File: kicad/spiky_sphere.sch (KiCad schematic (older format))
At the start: 0 parts

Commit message: filled in fixation target schematic
looks done... will review tomorrow
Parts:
- added JP? (x5): JUMPER, ~, symbol JUMPER
- added P?: CONN_8, ~, symbol CONN_8
- added U?: LED_MTX_5X7, symbol LED_MTX_5X7
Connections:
- new net: JP?.2, U?.2 (COL_1)
- new net: JP?.2, U?.1 (COL_2)
- new net: JP?.2, U?.4 (COL_3)
- new net: JP?.2, U?.9 (COL_4)
- new net: JP?.2, U?.7 (COL_5)
- new net fixation_target_module_1/GND: JP?.1, JP?.1, JP?.1, JP?.1, JP?.1, P?.8 (P8)
- new net fixation_target_module_1/V_IN: P?.1 (P1), U?.12 (ROW_1)
- new net fixation_target_module_2/V_IN: P?.2 (P2), U?.11 (ROW_2)
- new net fixation_target_module_3/V_IN: P?.3 (P3), U?.10 (ROW_3)
- new net fixation_target_module_4/V_IN: P?.4 (P4), U?.3 (ROW_4)
- new net fixation_target_module_5/V_IN: P?.5 (P5), U?.8 (ROW_5)
- new net fixation_target_module_6/V_IN: P?.6 (P6), U?.5 (ROW_6)
- new net fixation_target_module_7/V_IN: P?.7 (P7), U?.6 (ROW_7)
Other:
- note added: "0 ohm jumpers"
- note added: "<- to individual fixation boards w/ leads"
- note added: "LED MATRIX SPOOFER DROP-IN"
- note added: "pin-out of original LED MTX"
- note added: "really goes to bus XVR\nwhen on:\n-rows pulled high\n-cols pulled low"

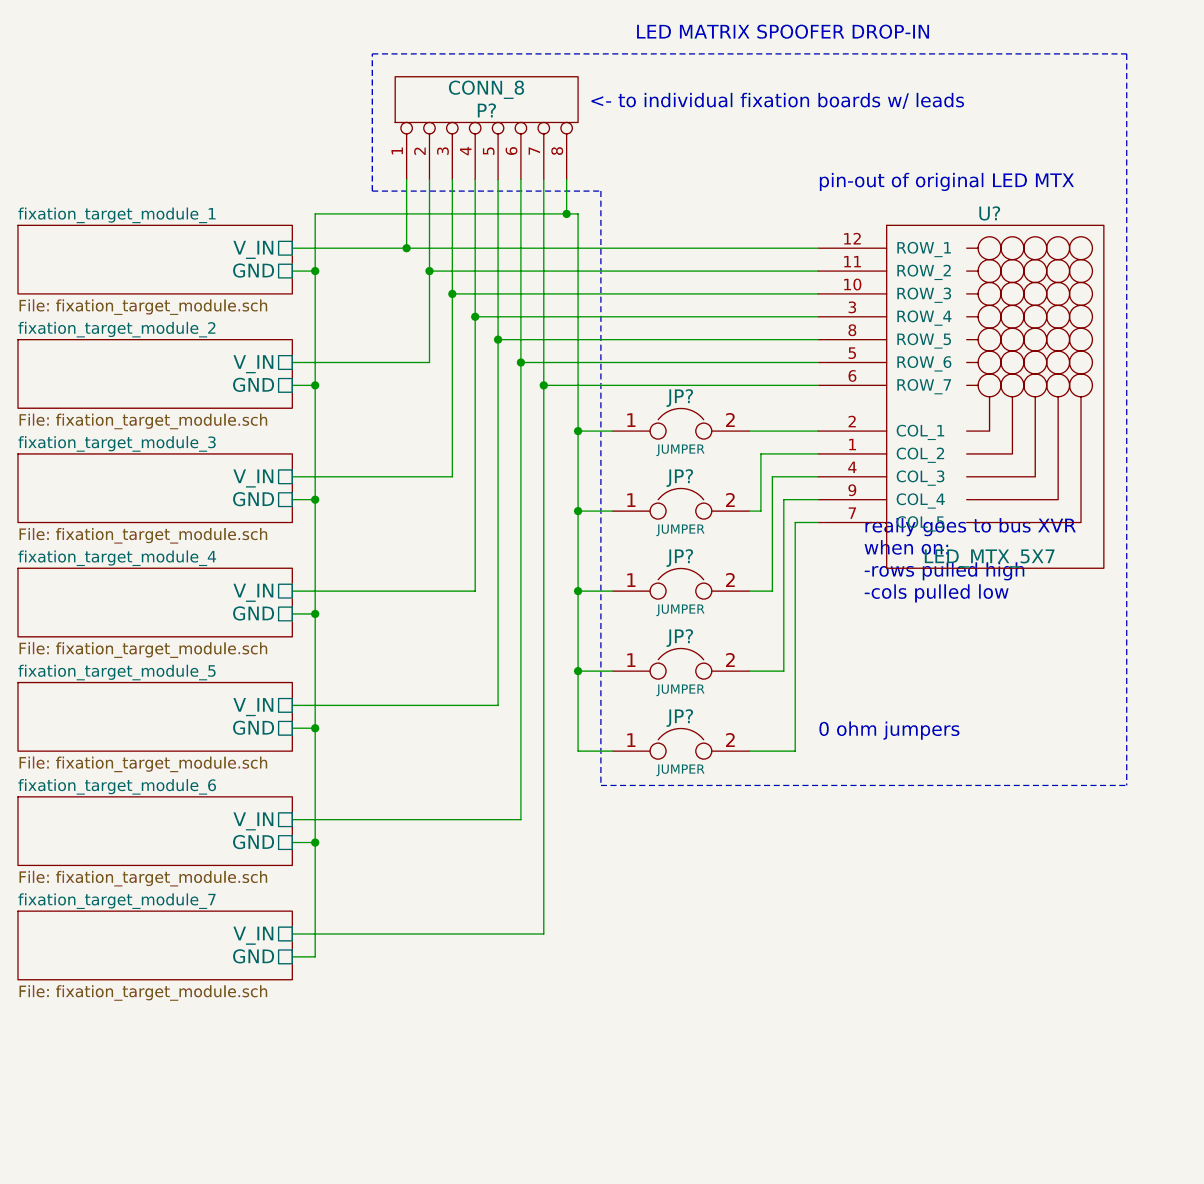
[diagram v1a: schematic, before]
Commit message: finished board v1.0
sent to freedfm for check
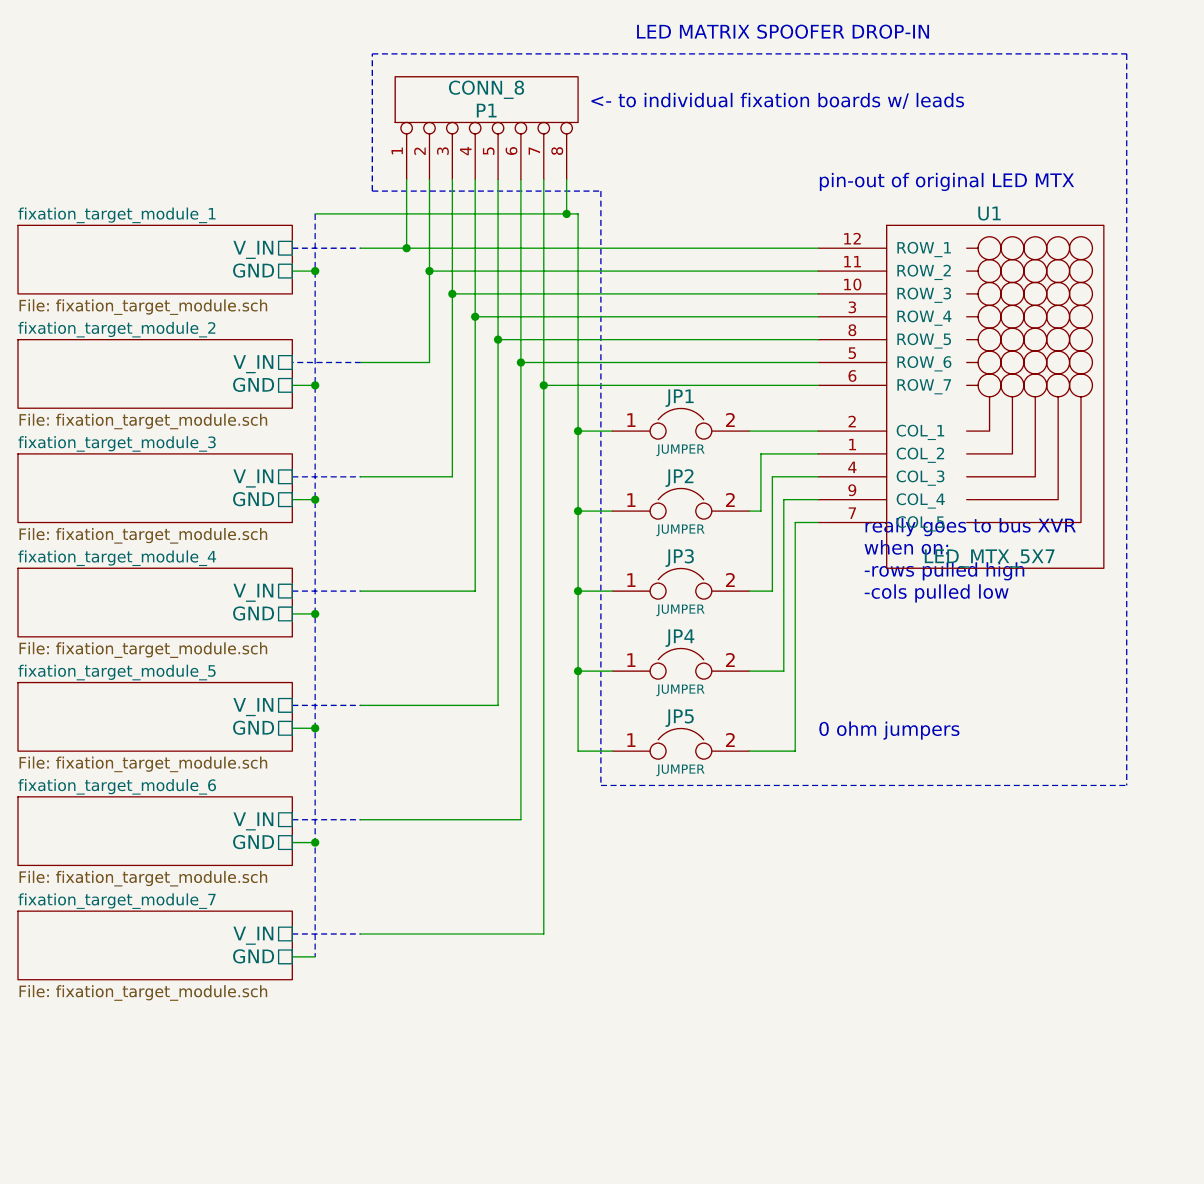
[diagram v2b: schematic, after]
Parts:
- gave numbers to parts that had none: 7
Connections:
- wire segments 67 -> 48
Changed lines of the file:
@@
 LIBS:contrib
 LIBS:valves
+LIBS:chroma_spotlight
 LIBS:spiky_sphere-cache
 EELAYER 27 0
@@
 $EndDescr
 $Comp
-L JUMPER JP?
+L JUMPER JP1
 U 1 1 52F19AD5
 P 6600 3400
-F 0 "JP?" H 6600 3550 60  0000 C CNN
+F 0 "JP1" H 6600 3550 60  0000 C CNN
 F 1 "JUMPER" H 6600 3320 40  0000 C CNN
 F 2 "~" H 6600 3400 60  0000 C CNN
@@
 $EndComp
 $Comp
-L JUMPER JP?
+L JUMPER JP2
 U 1 1 52F19AE2
 P 6600 3750
-F 0 "JP?" H 6600 3900 60  0000 C CNN
+F 0 "JP2" H 6600 3900 60  0000 C CNN
 F 1 "JUMPER" H 6600 3670 40  0000 C CNN
 F 2 "~" H 6600 3750 60  0000 C CNN
@@
 $EndComp
 $Comp
-L JUMPER JP?
+L JUMPER JP3
 U 1 1 52F19AE8
 P 6600 4100
-F 0 "JP?" H 6600 4250 60  0000 C CNN
+F 0 "JP3" H 6600 4250 60  0000 C CNN
 F 1 "JUMPER" H 6600 4020 40  0000 C CNN
 F 2 "~" H 6600 4100 60  0000 C CNN
@@
 $EndComp
 $Comp
-L JUMPER JP?
+L JUMPER JP4
 U 1 1 52F19AEE
 P 6600 4450
-F 0 "JP?" H 6600 4600 60  0000 C CNN
+F 0 "JP4" H 6600 4600 60  0000 C CNN
 F 1 "JUMPER" H 6600 4370 40  0000 C CNN
 F 2 "~" H 6600 4450 60  0000 C CNN
@@
 $EndComp
 $Comp
-L JUMPER JP?
+L JUMPER JP5
 U 1 1 52F19AF4
 P 6600 4800
-F 0 "JP?" H 6600 4950 60  0000 C CNN
+F 0 "JP5" H 6600 4950 60  0000 C CNN
 F 1 "JUMPER" H 6600 4720 40  0000 C CNN
 F 2 "~" H 6600 4800 60  0000 C CNN
@@
 $EndComp
 $Comp
-L LED_MTX_5X7 U?
+L LED_MTX_5X7 U1
 U 1 1 52F1A54C
 P 7950 2450
-F 0 "U?" H 7950 2450 60  0000 C CNN
+F 0 "U1" H 7950 2450 60  0000 C CNN
 F 1 "LED_MTX_5X7" H 7950 950 60  0000 C CNN
 F 2 "" H 7950 2450 60  0000 C CNN
@@
 LED MATRIX SPOOFER DROP-IN
 $Comp
-L CONN_8 P?
+L CONN_8 P1
 U 1 1 52F1A982
 P 5750 1950
-F 0 "P?" V 5700 1950 60  0000 C CNN
+F 0 "P1" V 5700 1950 60  0000 C CNN
 F 1 "CONN_8" V 5800 1950 60  0000 C CNN
 F 2 "~" H 5750 1950 60  0000 C CNN
@@
 	8550 1750 8550 4950
 Wire Wire Line
-	4900 2600 5400 2600
-Wire Wire Line
-	5400 2600 7200 2600
-Wire Wire Line
 	7200 2700 5500 2700
 Wire Wire Line
-	5500 2300 5500 2700
-Wire Wire Line
-	5500 2700 5500 3100
-Wire Wire Line
-	5500 3100 4900 3100
-Wire Wire Line
-	5600 3600 4900 3600
-Wire Wire Line
-	5600 2300 5600 2800
-Wire Wire Line
-	5600 2800 5600 3600
+	5500 2300 5500 3100
+Wire Wire Line
+	5600 2300 5600 3600
 Wire Wire Line
 	5600 2800 7200 2800
 Wire Wire Line
-	5700 4100 4900 4100
-Wire Wire Line
-	5700 2300 5700 2900
-Wire Wire Line
-	5700 2900 5700 4100
+	5700 2300 5700 4100
 Wire Wire Line
 	5700 2900 7200 2900
 Wire Wire Line
-	5800 4600 4900 4600
-Wire Wire Line
-	5800 2300 5800 3000
-Wire Wire Line
-	5800 3000 5800 4600
+	5800 2300 5800 4600
 Wire Wire Line
 	5800 3000 7200 3000
 Wire Wire Line
-	5900 5100 4900 5100
-Wire Wire Line
-	5900 2300 5900 3100
-Wire Wire Line
-	5900 3100 5900 5100
+	5900 2300 5900 5100
 Wire Wire Line
 	5900 3100 7200 3100
 Wire Wire Line
-	6000 5600 4900 5600
-Wire Wire Line
-	6000 2300 6000 3200
-Wire Wire Line
-	6000 3200 6000 5600
+	6000 2300 6000 5600
 Wire Wire Line
 	6000 3200 7200 3200
@@
 Connection ~ 5000 2700
 Wire Wire Line
-	5000 2450 5000 2700
-Wire Wire Line
-	5000 2700 5000 3200
-Wire Wire Line
-	5000 3200 5000 3700
-Wire Wire Line
-	5000 3700 5000 4200
-Wire Wire Line
-	5000 4200 5000 4700
-Wire Wire Line
-	5000 4700 5000 5200
-Wire Wire Line
-	5000 5200 5000 5700
-Wire Wire Line
-	5000 2450 6100 2450
-Wire Wire Line
-	6100 2450 6150 2450
+	5000 2450 6150 2450
 Wire Wire Line
 	5400 2300 5400 2600
@@
 	6100 2450 6100 2300
 Wire Wire Line
-	6150 2450 6150 3400
-Wire Wire Line
-	6150 3400 6150 3750
-Wire Wire Line
-	6150 3750 6150 4100
-Wire Wire Line
-	6150 4100 6150 4450
-Wire Wire Line
-	6150 4450 6150 4800
+	6150 2450 6150 4800
 Text Notes 6200 2000 0    60   ~ 0
 <- to individual fixation boards w/ leads
@@
 Text Notes 7400 4150 0    60   ~ 0
 really goes to bus XVR\nwhen on:\n-rows pulled high\n-cols pulled low
+Wire Notes Line
+	5000 2450 5000 5700
+Wire Wire Line
+	5200 2600 7200 2600
+Wire Wire Line
+	5500 3100 5200 3100
+Wire Wire Line
+	5600 3600 5200 3600
+Wire Wire Line
+	5700 4100 5200 4100
+Wire Wire Line
+	5800 4600 5200 4600
+Wire Wire Line
+	5900 5100 5200 5100
+Wire Wire Line
+	6000 5600 5200 5600
+Wire Notes Line
+	4900 2600 5200 2600
+Wire Notes Line
+	5200 3100 4900 3100
+Wire Notes Line
+	4900 3600 5200 3600
+Wire Notes Line
+	4900 4100 5200 4100
+Wire Notes Line
+	4900 4600 5200 4600
+Wire Notes Line
+	4900 5100 5200 5100
+Wire Notes Line
+	4900 5600 5200 5600
 $EndSCHEMATC

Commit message: small changes and added illum boards
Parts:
- added D22: XP-E2_LED, ~, symbol XP-E2_LED
- added K8: CONN_3, ~, symbol CONN_3
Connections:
- net labels added: GND, V_IN
- wire segments 48 -> 55
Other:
- note added: "Board for illumination LED"
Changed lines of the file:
@@
 Sheet 1 8
 Title "Fixation Target System"
-Date "5 feb 2014"
+Date "6 feb 2014"
 Rev "V 1.0"
 Comp "Rice University"
@@
 Wire Notes Line
 	4900 5600 5200 5600
+$Comp
+L CONN_3 K8
+U 1 1 52F3DE49
+P 7250 5650
+F 0 "K8" V 7200 5650 50  0000 C CNN
+F 1 "CONN_3" V 7300 5650 40  0000 C CNN
+F 2 "~" H 7250 5650 60  0000 C CNN
+F 3 "~" H 7250 5650 60  0000 C CNN
+	1    7250 5650
+	-1   0    0    -1
+$EndComp
+Wire Wire Line
+	7600 5650 7600 6550
+Wire Wire Line
+	7600 6550 8050 6550
+Connection ~ 7600 5750
+Wire Wire Line
+	7600 5550 7950 5550
+Wire Wire Line
+	7850 5550 8050 5550
+Connection ~ 7850 5550
+Connection ~ 7850 6550
+Text HLabel 8050 5550 2    60   UnSpc ~ 0
+V_IN
+Text HLabel 8050 6550 2    60   UnSpc ~ 0
+GND
+$Comp
+L XP-E2_LED D22
+U 1 1 52F3E073
+P 7850 5750
+F 0 "D22" H 7850 5850 50  0000 C CNN
+F 1 "XP-E2_LED" H 7850 5650 50  0001 C CNN
+F 2 "~" H 7850 5750 60  0000 C CNN
+F 3 "~" H 7850 5750 60  0000 C CNN
+	1    7850 5750
+	0    1    1    0
+$EndComp
+Wire Wire Line
+	7850 5950 7850 6550
+Wire Wire Line
+	7900 5800 7900 5950
+Wire Wire Line
+	7900 5950 7850 5950
+Wire Notes Line
+	7100 5450 8350 5450
+Wire Notes Line
+	8350 5450 8350 6600
+Wire Notes Line
+	8350 6600 7100 6600
+Wire Notes Line
+	7100 6600 7100 5450
+Text Notes 7100 5450 0    60   ~ 0
+Board for illumination LED
 $EndSCHEMATC
